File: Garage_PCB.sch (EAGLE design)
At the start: 19 parts, among them Q1 MOSFET-NCHANNELFQP30N06L

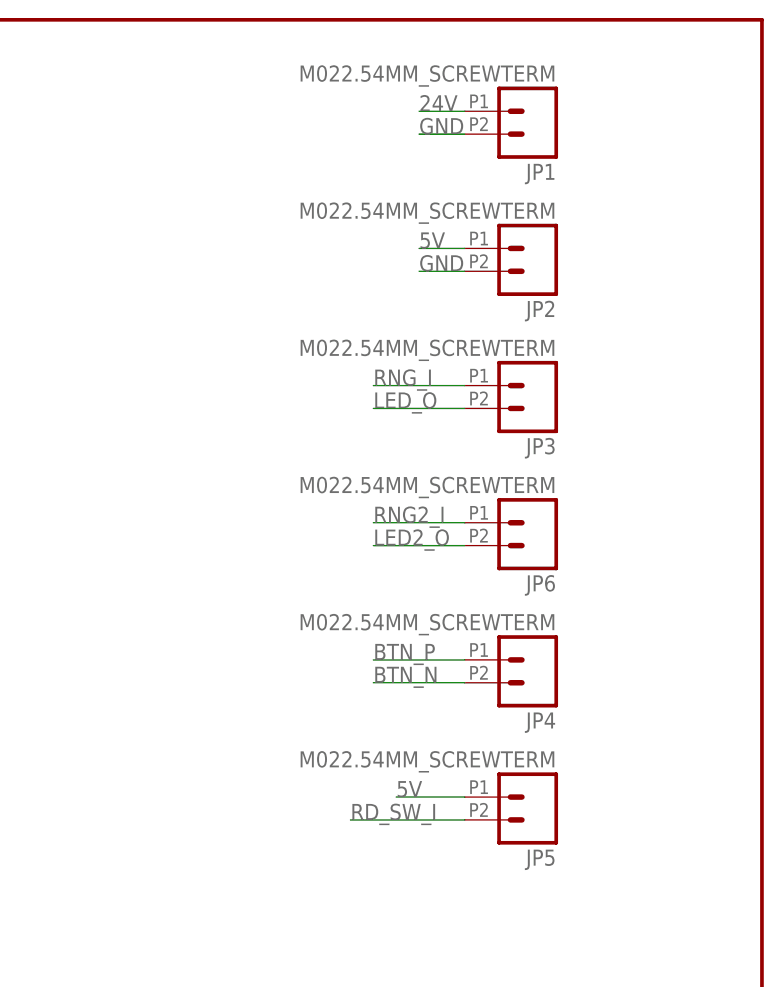
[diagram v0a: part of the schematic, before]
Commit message: Changed screw terminals to 3.5mm pitch instead of 2.54mm
These screw terminals are much less ugly but are a bit bigger.  They
still fit pretty well though.
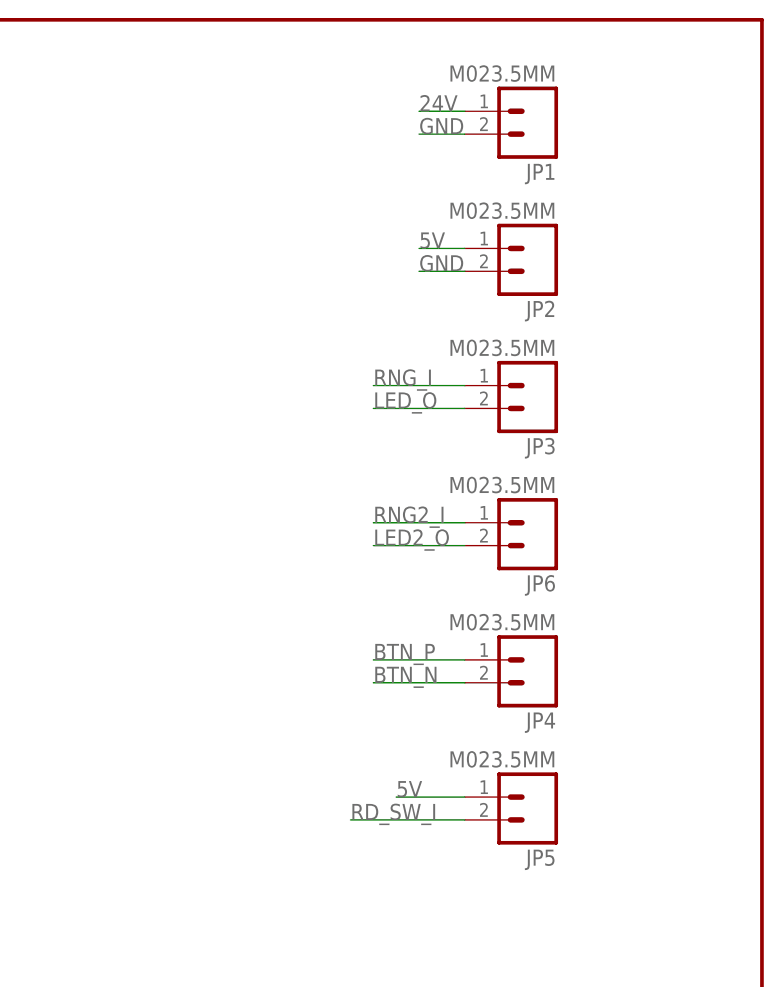
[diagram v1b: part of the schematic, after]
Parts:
- JP1, JP2, JP3, JP4, JP5, JP6: value M022.54MM_SCREWTERM -> M023.5MM; device Mikes-Stuff:M022.54MM_SCREWTERM -> SparkFun-Connectors:M023.5MM
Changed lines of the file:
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@@
 <part name="SUPPLY2" library="SparkFun-Aesthetics" deviceset="5V" device=""/>
 <part name="U$1" library="Spark" deviceset="SPARK_CORE" device="CORE"/>
-<part name="JP1" library="Mikes-Stuff" deviceset="M02" device="2.54MM_SCREWTERM"/>
-<part name="JP2" library="Mikes-Stuff" deviceset="M02" device="2.54MM_SCREWTERM"/>
-<part name="JP3" library="Mikes-Stuff" deviceset="M02" device="2.54MM_SCREWTERM"/>
-<part name="JP4" library="Mikes-Stuff" deviceset="M02" device="2.54MM_SCREWTERM"/>
+<part name="JP1" library="SparkFun-Connectors" deviceset="M02" device="3.5MM"/>
+<part name="JP2" library="SparkFun-Connectors" deviceset="M02" device="3.5MM"/>
+<part name="JP3" library="SparkFun-Connectors" deviceset="M02" device="3.5MM"/>
+<part name="JP4" library="SparkFun-Connectors" deviceset="M02" device="3.5MM"/>
 <part name="Q1" library="SparkFun-DiscreteSemi" deviceset="MOSFET-NCHANNEL" device="FQP30N06L"/>
 <part name="R1" library="SparkFun-Resistors" deviceset="RESISTOR" device="0603" value="10K"/>
@@
 <part name="C2" library="SparkFun-Capacitors" deviceset="CAP" device="0603-CAP"/>
 <part name="R2" library="SparkFun-Resistors" deviceset="RESISTOR" device="0603" value="1K"/>
-<part name="JP5" library="Mikes-Stuff" deviceset="M02" device="2.54MM_SCREWTERM"/>
+<part name="JP5" library="SparkFun-Connectors" deviceset="M02" device="3.5MM"/>
 <part name="R3" library="SparkFun-Resistors" deviceset="RESISTOR" device="0603"/>
 <part name="STANDOFF1" library="SparkFun-Electromechanical" deviceset="STAND-OFF" device=""/>
@@
 <part name="STANDOFF3" library="SparkFun-Electromechanical" deviceset="STAND-OFF" device=""/>
 <part name="STANDOFF4" library="SparkFun-Electromechanical" deviceset="STAND-OFF" device=""/>
-<part name="JP6" library="Mikes-Stuff" deviceset="M02" device="2.54MM_SCREWTERM"/>
+<part name="JP6" library="SparkFun-Connectors" deviceset="M02" device="3.5MM"/>
 </parts>
 <sheets>

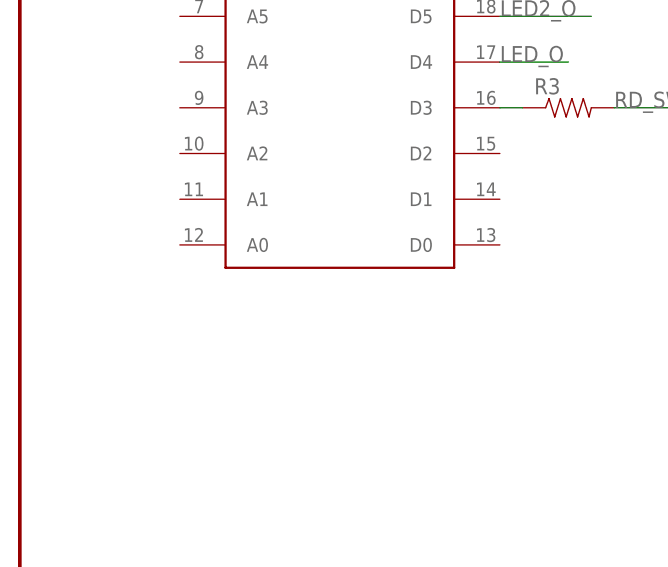
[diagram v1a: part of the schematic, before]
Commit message: Added my name and the Spark logo
Added my name to the board and the Spark logo as well.  Also added the
Spark Eagle Library to the Eagle directory search paths so that I can
edit library parts.
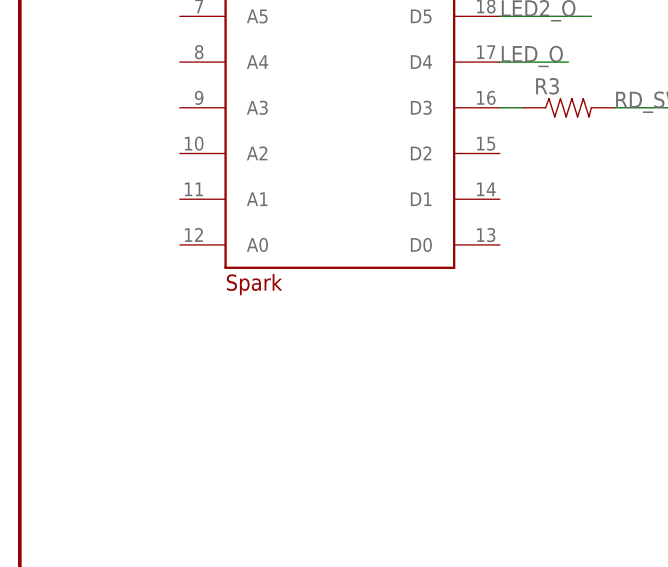
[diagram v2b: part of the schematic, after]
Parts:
- added U$2: SPARK_LOGO2, Spark:SPARK_LOGO2
- renumbered U$1 to SPARK
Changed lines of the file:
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@@
 <layer number="19" name="Unrouted" color="6" fill="1" visible="no" active="no"/>
 <layer number="20" name="Dimension" color="15" fill="1" visible="no" active="no"/>
-<layer number="21" name="tPlace" color="7" fill="1" visible="no" active="no"/>
-<layer number="22" name="bPlace" color="7" fill="1" visible="no" active="no"/>
+<layer number="21" name="tPlace" color="16" fill="1" visible="no" active="no"/>
+<layer number="22" name="bPlace" color="14" fill="1" visible="no" active="no"/>
 <layer number="23" name="tOrigins" color="15" fill="1" visible="no" active="no"/>
 <layer number="24" name="bOrigins" color="15" fill="1" visible="no" active="no"/>
@@
 <layer number="49" name="Reference" color="7" fill="1" visible="no" active="no"/>
 <layer number="50" name="dxf" color="7" fill="1" visible="no" active="no"/>
-<layer number="51" name="tDocu" color="7" fill="1" visible="no" active="no"/>
+<layer number="51" name="tDocu" color="6" fill="1" visible="no" active="no"/>
 <layer number="52" name="bDocu" color="7" fill="1" visible="no" active="no"/>
 <layer number="53" name="tGND_GNDA" color="7" fill="9" visible="no" active="no"/>
@@
 <part name="SUPPLY1" library="SparkFun-Aesthetics" deviceset="3.3V" device=""/>
 <part name="SUPPLY2" library="SparkFun-Aesthetics" deviceset="5V" device=""/>
-<part name="U$1" library="Spark" deviceset="SPARK_CORE" device="CORE"/>
+<part name="SPARK" library="Spark" deviceset="SPARK_CORE" device="CORE"/>
 <part name="JP1" library="SparkFun-Connectors" deviceset="M02" device="3.5MM"/>
 <part name="JP2" library="SparkFun-Connectors" deviceset="M02" device="3.5MM"/>
@@
 <part name="STANDOFF4" library="SparkFun-Electromechanical" deviceset="STAND-OFF" device=""/>
 <part name="JP6" library="SparkFun-Connectors" deviceset="M02" device="3.5MM"/>
+<part name="U$2" library="Spark" deviceset="SPARK_LOGO2" device=""/>
 </parts>
 <sheets>
@@
 <instance part="SUPPLY1" gate="G$1" x="114.3" y="10.16"/>
 <instance part="SUPPLY2" gate="G$1" x="109.22" y="10.16"/>
-<instance part="U$1" gate="G$1" x="35.56" y="147.32"/>
+<instance part="SPARK" gate="G$1" x="35.56" y="147.32"/>
 <instance part="JP1" gate="G$1" x="223.52" y="175.26" rot="R180"/>
 <instance part="JP2" gate="G$1" x="223.52" y="160.02" rot="R180"/>
@@
 <instance part="STANDOFF4" gate="G$1" x="78.74" y="10.16"/>
 <instance part="JP6" gate="G$1" x="223.52" y="129.54" rot="R180"/>
+<instance part="U$2" gate="G$1" x="22.86" y="114.3"/>
 </instances>
 <busses>
@@
 </segment>
 <segment>
-<pinref part="U$1" gate="G$1" pin="D4"/>
+<pinref part="SPARK" gate="G$1" pin="D4"/>
 <wire x1="53.34" y1="139.7" x2="60.96" y2="139.7" width="0.2032" layer="91"/>
 <label x="53.34" y="139.7" size="1.778" layer="95"/>
@@
 <net name="3.3V" class="0">
 <segment>
-<pinref part="U$1" gate="G$1" pin="VCC"/>
+<pinref part="SPARK" gate="G$1" pin="VCC"/>
 <wire x1="53.34" y1="175.26" x2="58.42" y2="175.26" width="0.2032" layer="91"/>
 <label x="53.34" y="175.26" size="1.778" layer="95"/>
@@
 <net name="N$15" class="0">
 <segment>
-<pinref part="U$1" gate="G$1" pin="D6"/>
+<pinref part="SPARK" gate="G$1" pin="D6"/>
 <wire x1="53.34" y1="149.86" x2="76.2" y2="149.86" width="0.2032" layer="91"/>
 <wire x1="76.2" y1="149.86" x2="76.2" y2="157.48" width="0.2032" layer="91"/>
@@
 <net name="RNG_I" class="0">
 <segment>
-<pinref part="U$1" gate="G$1" pin="A6"/>
+<pinref part="SPARK" gate="G$1" pin="A6"/>
 <wire x1="17.78" y1="149.86" x2="10.16" y2="149.86" width="0.2032" layer="91"/>
 <label x="10.16" y="149.86" size="1.778" layer="95"/>
@@
 </segment>
 <segment>
-<pinref part="U$1" gate="G$1" pin="GND@2"/>
+<pinref part="SPARK" gate="G$1" pin="GND@2"/>
 <wire x1="17.78" y1="170.18" x2="12.7" y2="170.18" width="0.2032" layer="91"/>
 <label x="12.7" y="170.18" size="1.778" layer="95"/>
 </segment>
 <segment>
-<pinref part="U$1" gate="G$1" pin="GND@21"/>
+<pinref part="SPARK" gate="G$1" pin="GND@21"/>
 <wire x1="53.34" y1="160.02" x2="58.42" y2="160.02" width="0.2032" layer="91"/>
 <label x="53.34" y="160.02" size="1.778" layer="95"/>
@@
 </segment>
 <segment>
-<pinref part="U$1" gate="G$1" pin="RAW"/>
+<pinref part="SPARK" gate="G$1" pin="RAW"/>
 <wire x1="17.78" y1="175.26" x2="12.7" y2="175.26" width="0.2032" layer="91"/>
 <label x="12.7" y="175.26" size="1.778" layer="95"/>
@@
 <net name="N$1" class="0">
 <segment>
-<pinref part="U$1" gate="G$1" pin="D3"/>
+<pinref part="SPARK" gate="G$1" pin="D3"/>
 <pinref part="R3" gate="G$1" pin="1"/>
 <wire x1="53.34" y1="134.62" x2="55.88" y2="134.62" width="0.2032" layer="91"/>
@@
 </segment>
 <segment>
-<pinref part="U$1" gate="G$1" pin="A7"/>
+<pinref part="SPARK" gate="G$1" pin="A7"/>
 <wire x1="17.78" y1="154.94" x2="10.16" y2="154.94" width="0.2032" layer="91"/>
 <label x="10.16" y="154.94" size="1.778" layer="95"/>
@@
 <net name="LED2_O" class="0">
 <segment>
-<pinref part="U$1" gate="G$1" pin="D5"/>
+<pinref part="SPARK" gate="G$1" pin="D5"/>
 <wire x1="53.34" y1="144.78" x2="63.5" y2="144.78" width="0.2032" layer="91"/>
 <label x="53.34" y="144.78" size="1.778" layer="95"/>

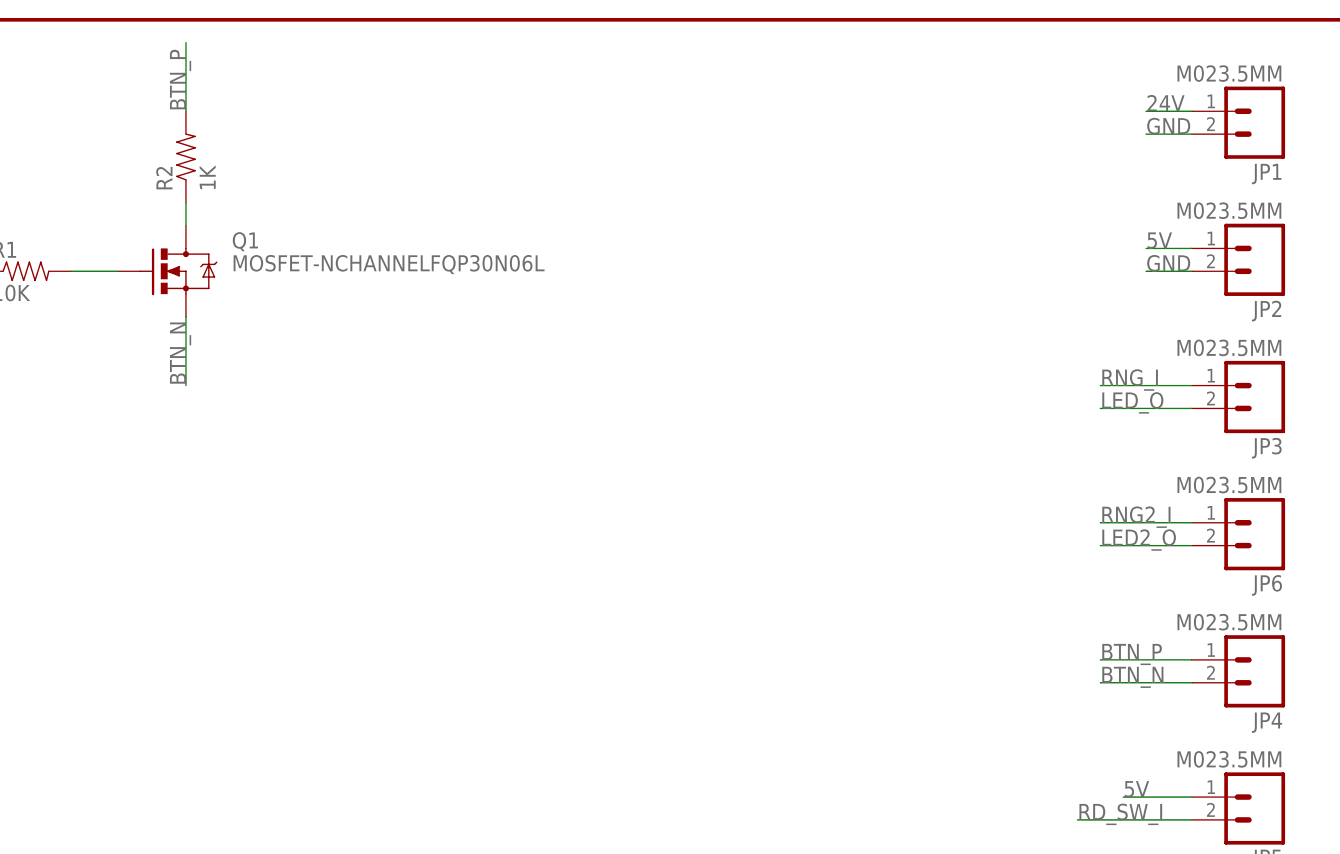
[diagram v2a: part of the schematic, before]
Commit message: Moved Mosfet and shrunk design
Moved the MOSFET underneath the Spark on the bottom layer so I can save
some space.  I moved just about everything around and was able to shrink
the board down to basically just the size of the Spark and the extra
width of the screw terminals.  It is very small now and costs almost $4
less to build.
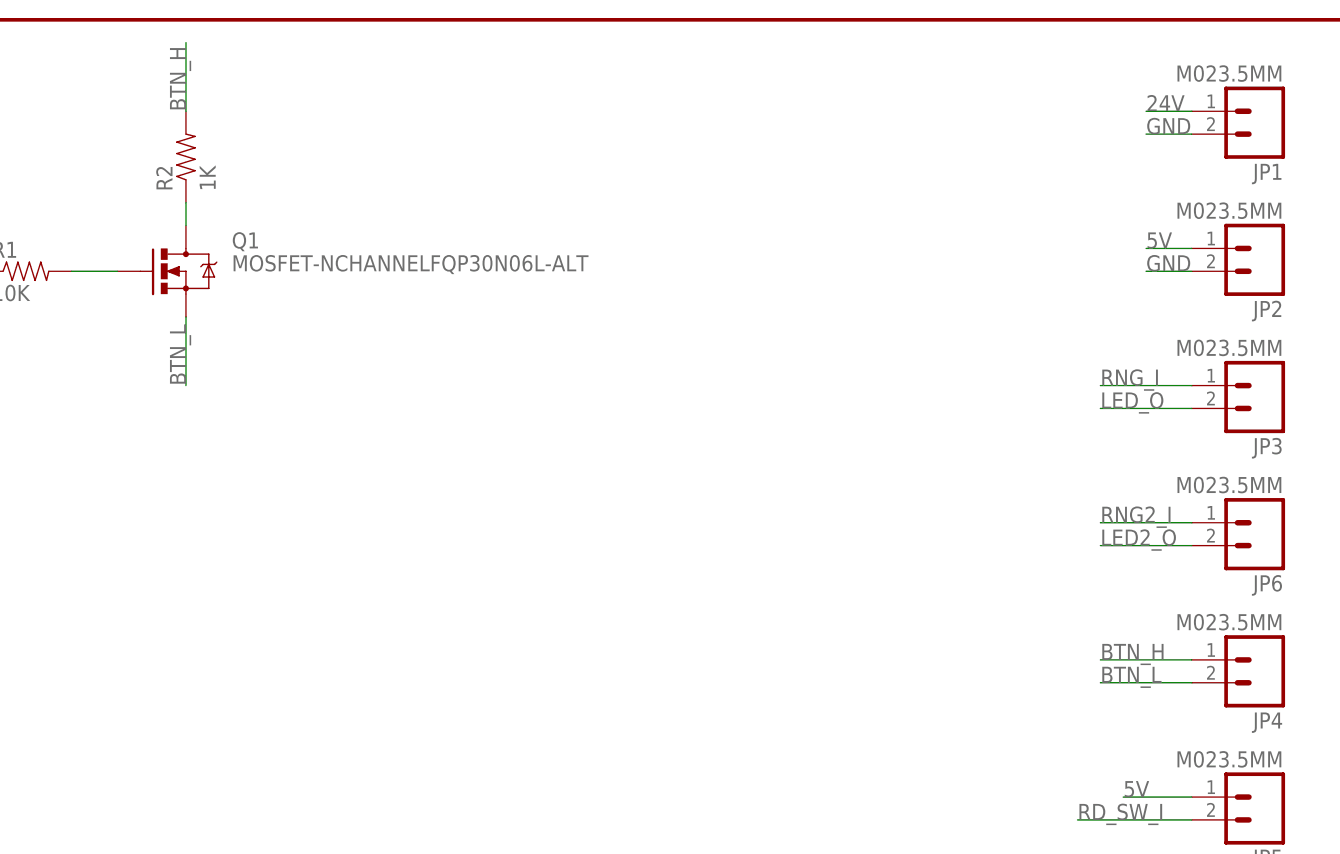
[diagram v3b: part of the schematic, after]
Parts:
- Q1: value MOSFET-NCHANNELFQP30N06L -> MOSFET-NCHANNELFQP30N06L-ALT; device SparkFun-DiscreteSemi:MOSFET-NCHANNELFQP30N06L -> SparkFun-DiscreteSemi:MOSFET-NCHANNELFQP30N06L-ALT
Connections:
- net BTN_N renamed BTN_L
- net BTN_P renamed BTN_H
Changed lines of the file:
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@@
 <part name="JP3" library="SparkFun-Connectors" deviceset="M02" device="3.5MM"/>
 <part name="JP4" library="SparkFun-Connectors" deviceset="M02" device="3.5MM"/>
-<part name="Q1" library="SparkFun-DiscreteSemi" deviceset="MOSFET-NCHANNEL" device="FQP30N06L"/>
+<part name="Q1" library="SparkFun-DiscreteSemi" deviceset="MOSFET-NCHANNEL" device="FQP30N06L-ALT" value="MOSFET-NCHANNELFQP30N06L-ALT"/>
 <part name="R1" library="SparkFun-Resistors" deviceset="RESISTOR" device="0603" value="10K"/>
 <part name="24V" library="SparkFun-Aesthetics" deviceset="VCC" device="" value="24V"/>
@@
 </busses>
 <nets>
-<net name="BTN_P" class="0">
-<segment>
-<pinref part="JP4" gate="G$1" pin="1"/>
-<wire x1="215.9" y1="114.3" x2="205.74" y2="114.3" width="0.2032" layer="91"/>
-<label x="205.74" y="114.3" size="1.778" layer="95"/>
-</segment>
-<segment>
-<pinref part="R2" gate="G$1" pin="2"/>
-<wire x1="104.14" y1="175.26" x2="104.14" y2="182.88" width="0.2032" layer="91"/>
-<label x="104.14" y="175.26" size="1.778" layer="95" rot="R90"/>
-</segment>
-</net>
-<net name="BTN_N" class="0">
-<segment>
-<pinref part="JP4" gate="G$1" pin="2"/>
-<wire x1="215.9" y1="111.76" x2="205.74" y2="111.76" width="0.2032" layer="91"/>
-<label x="205.74" y="111.76" size="1.778" layer="95"/>
-</segment>
-<segment>
-<pinref part="Q1" gate="G$1" pin="S"/>
-<wire x1="104.14" y1="152.4" x2="104.14" y2="144.78" width="0.2032" layer="91"/>
-<label x="104.14" y="144.78" size="1.778" layer="95" rot="R90"/>
-</segment>
-</net>
 <net name="LED_O" class="0">
 <segment>
@@
 </segment>
 </net>
+<net name="BTN_H" class="0">
+<segment>
+<pinref part="JP4" gate="G$1" pin="1"/>
+<wire x1="215.9" y1="114.3" x2="205.74" y2="114.3" width="0.2032" layer="91"/>
+<label x="205.74" y="114.3" size="1.778" layer="95"/>
+</segment>
+<segment>
+<pinref part="R2" gate="G$1" pin="2"/>
+<wire x1="104.14" y1="175.26" x2="104.14" y2="182.88" width="0.2032" layer="91"/>
+<label x="104.14" y="175.26" size="1.778" layer="95" rot="R90"/>
+</segment>
+</net>
+<net name="BTN_L" class="0">
+<segment>
+<pinref part="JP4" gate="G$1" pin="2"/>
+<wire x1="215.9" y1="111.76" x2="205.74" y2="111.76" width="0.2032" layer="91"/>
+<label x="205.74" y="111.76" size="1.778" layer="95"/>
+</segment>
+<segment>
+<pinref part="Q1" gate="G$1" pin="S"/>
+<wire x1="104.14" y1="152.4" x2="104.14" y2="144.78" width="0.2032" layer="91"/>
+<label x="104.14" y="144.78" size="1.778" layer="95" rot="R90"/>
+</segment>
+</net>
